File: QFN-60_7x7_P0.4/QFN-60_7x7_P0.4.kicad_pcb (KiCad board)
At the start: 2 copper layers, 25.4 x 81.3 mm, 6 parts, among them J101 Conn_01x32, J102 Conn_01x32, J103 Conn_01x32, J104 Conn_01x32, U101 QFN-60

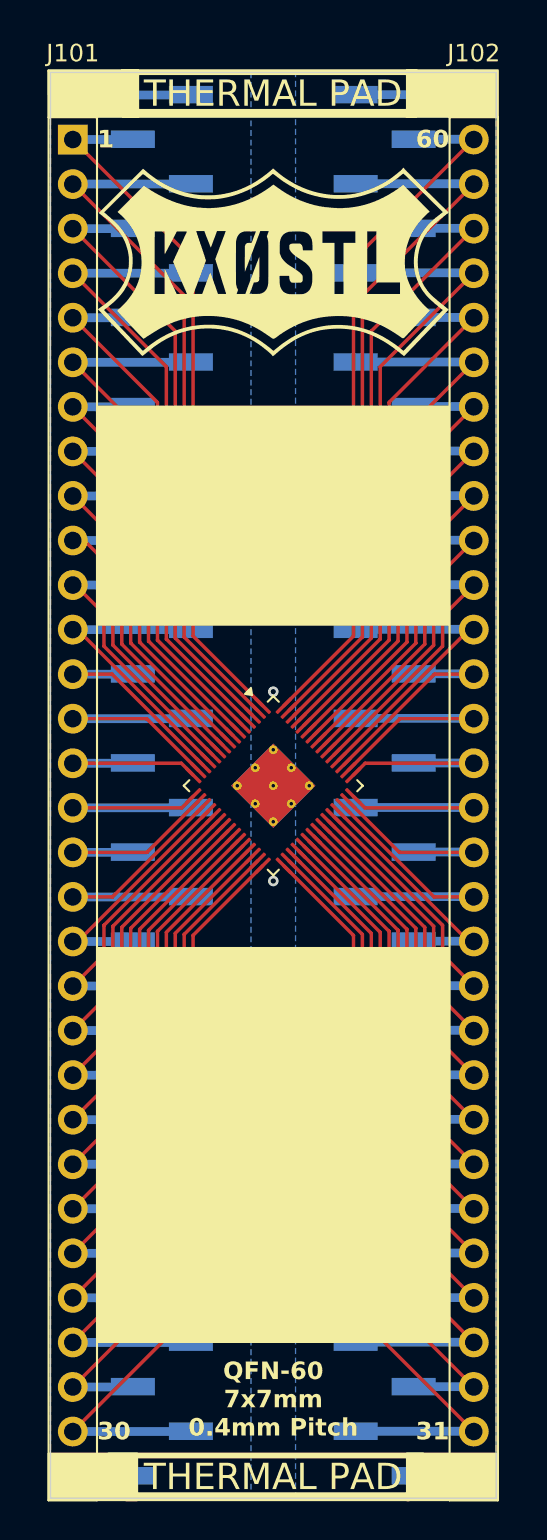
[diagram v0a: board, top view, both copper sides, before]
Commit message: Created SMDIP-16, QFP-48, QFP-32, QFN-80, QFN-68, QFN-64, QFN-60, QFN-56, QFN-48, QFN-36, QFN-28, QFN-20, QFP-32, QFP-48
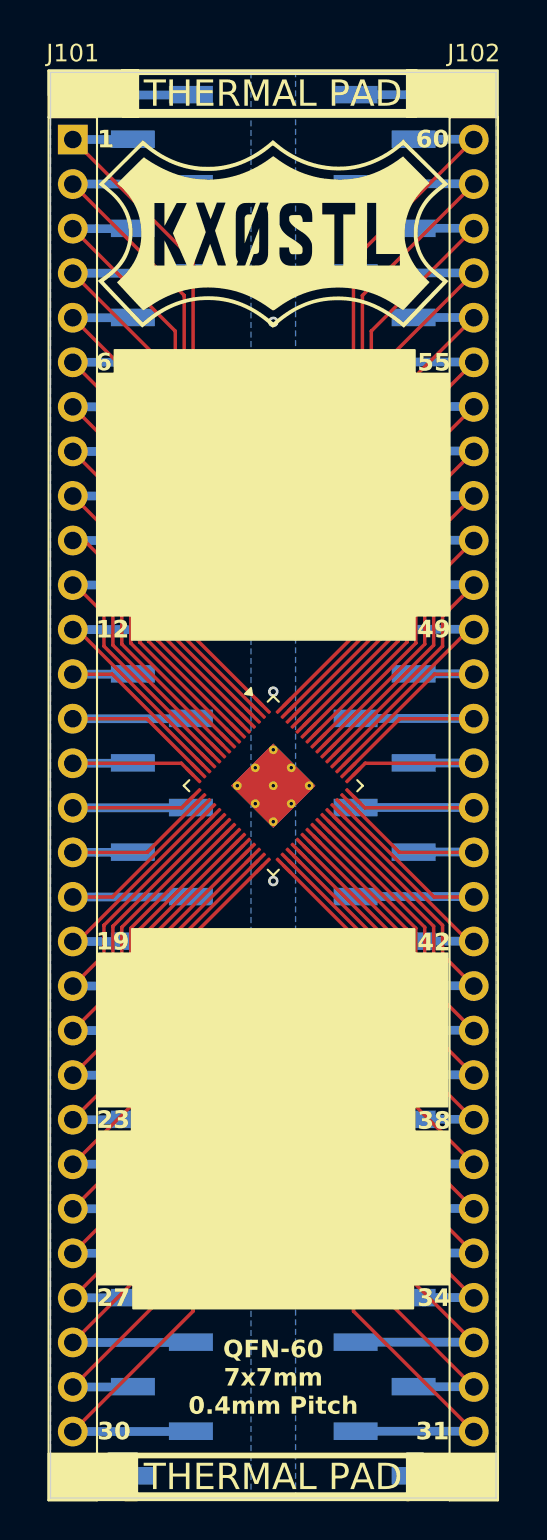
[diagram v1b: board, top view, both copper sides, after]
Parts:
- moved G*** 1.62 mm to (138.4, 89.3)
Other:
- board text added: "12"
- board text added: "19"
- board text added: "23"
- board text added: "27"
- board text added: "34"
- board text added: "38"
- board text added: "42"
- board text added: "49"
- board text added: "55"
- board text added: "6"
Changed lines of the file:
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@@
 	(footprint "libraries:LogoSmall"
 		(layer "F.Cu")
-		(at 138.43 90.949121)
+		(at 138.42 89.327121)
 		(property "Reference" "G***"
 			(at 0 0 0)
@@
 	)
 	(gr_rect
-		(start 128.397 130.048)
-		(end 148.463 152.527)
+		(start 128.397 140.5105)
+		(end 148.463 149.247)
+		(stroke
+			(width 0.1)
+			(type solid)
+		)
+		(fill yes)
+		(layer "F.SilkS")
+	)
+	(gr_rect
+		(start 130.437 149.241)
+		(end 146.413 150.6155)
 		(stroke
 			(width 0.1)
@@
 	)
 	(gr_rect
+		(start 130.357 128.97)
+		(end 146.483 140.76175)
+		(stroke
+			(width 0.1)
+			(type solid)
+		)
+		(fill yes)
+		(layer "F.SilkS")
+	)
+	(gr_rect
+		(start 128.474 130.359125)
+		(end 148.37 139.100875)
+		(stroke
+			(width 0.1)
+			(type solid)
+		)
+		(fill yes)
+		(layer "F.SilkS")
+	)
+	(gr_rect
 		(start 129.0235 158.87675)
 		(end 146.98125 159.1051)
@@
 	)
 	(gr_rect
-		(start 128.397 99.187)
-		(end 148.463 111.633)
+		(start 128.397 97.307)
+		(end 148.463 111.113)
+		(stroke
+			(width 0.1)
+			(type solid)
+		)
+		(fill yes)
+		(layer "F.SilkS")
+	)
+	(gr_rect
+		(start 130.357 98.687)
+		(end 146.503 112.493)
 		(stroke
 			(width 0.1)
@@
 	)
 	(gr_rect
+		(start 129.377 95.96)
+		(end 146.503 98.08)
+		(stroke
+			(width 0.1)
+			(type solid)
+		)
+		(fill yes)
+		(layer "F.SilkS")
+	)
+	(gr_rect
 		(start 125.73 80.137)
 		(end 151.13 161.417)
@@
 		)
 	)
+	(gr_text "23"
+		(at 128.35 139.85 0)
+		(layer "F.SilkS" knockout)
+		(effects
+			(font
+				(size 1 1)
+				(thickness 0.2)
+				(bold yes)
+			)
+			(justify left)
+		)
+	)
 	(gr_text "31"
 		(at 148.463 157.607 0)
@@
 		)
 	)
+	(gr_text "12"
+		(at 128.31 111.89 0)
+		(layer "F.SilkS" knockout)
+		(effects
+			(font
+				(size 1 1)
+				(thickness 0.2)
+				(bold yes)
+			)
+			(justify left)
+		)
+	)
 	(gr_text "THERMAL PAD"
 		(at 138.4215 81.343625 0)
@@
 	)
 	(gr_text "QFN-60\n7x7mm\n0.4mm Pitch"
-		(at 138.43 157.975944 0)
+		(at 138.43 156.733532 0)
 		(layer "F.SilkS")
 		(effects
@@
 		)
 	)
+	(gr_text "55"
+		(at 148.55 96.67 0)
+		(layer "F.SilkS" knockout)
+		(effects
+			(font
+				(size 1 1)
+				(thickness 0.2)
+				(bold yes)
+			)
+			(justify right)
+		)
+	)
 	(gr_text "30"
 		(at 128.397 157.607 0)
@@
 		)
 	)
+	(gr_text "6"
+		(at 128.28 96.66 0)
+		(layer "F.SilkS" knockout)
+		(effects
+			(font
+				(size 1 1)
+				(thickness 0.2)
+				(bold yes)
+			)
+			(justify left)
+		)
+	)
+	(gr_text "19"
+		(at 128.32 129.68 0)
+		(layer "F.SilkS" knockout)
+		(effects
+			(font
+				(size 1 1)
+				(thickness 0.2)
+				(bold yes)
+			)
+			(justify left)
+		)
+	)
+	(gr_text "38"
+		(at 148.55 139.9 0)
+		(layer "F.SilkS" knockout)
+		(effects
+			(font
+				(size 1 1)
+				(thickness 0.2)
+				(bold yes)
+			)
+			(justify right)
+		)
+	)
 	(gr_text "1"
 		(at 128.397 83.947 0)
@@
 		)
 	)
+	(gr_text "34"
+		(at 148.54 150 0)
+		(layer "F.SilkS" knockout)
+		(effects
+			(font
+				(size 1 1)
+				(thickness 0.2)
+				(bold yes)
+			)
+			(justify right)
+		)
+	)
+	(gr_text "27"
+		(at 128.36 150 0)
+		(layer "F.SilkS" knockout)
+		(effects
+			(font
+				(size 1 1)
+				(thickness 0.2)
+				(bold yes)
+			)
+			(justify left)
+		)
+	)
+	(gr_text "42"
+		(at 148.55 129.726271 0)
+		(layer "F.SilkS" knockout)
+		(effects
+			(font
+				(size 1 1)
+				(thickness 0.2)
+				(bold yes)
+			)
+			(justify right)
+		)
+	)
+	(gr_text "49"
+		(at 148.54 111.88 0)
+		(layer "F.SilkS" knockout)
+		(effects
+			(font
+				(size 1 1)
+				(thickness 0.2)
+				(bold yes)
+			)
+			(justify right)
+		)
+	)
